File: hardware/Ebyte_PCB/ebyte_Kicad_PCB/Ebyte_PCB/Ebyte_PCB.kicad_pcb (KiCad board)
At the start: 2 copper layers, 31 parts, among them Q1 NPN, Q2 PMOS, U1 DF11, U2 LT8612IUDE, U3 E32-400M33S SX1278, U4 MIC69303RT, U5 CONMMCX001, U6 SN74LVC1G08DBVR

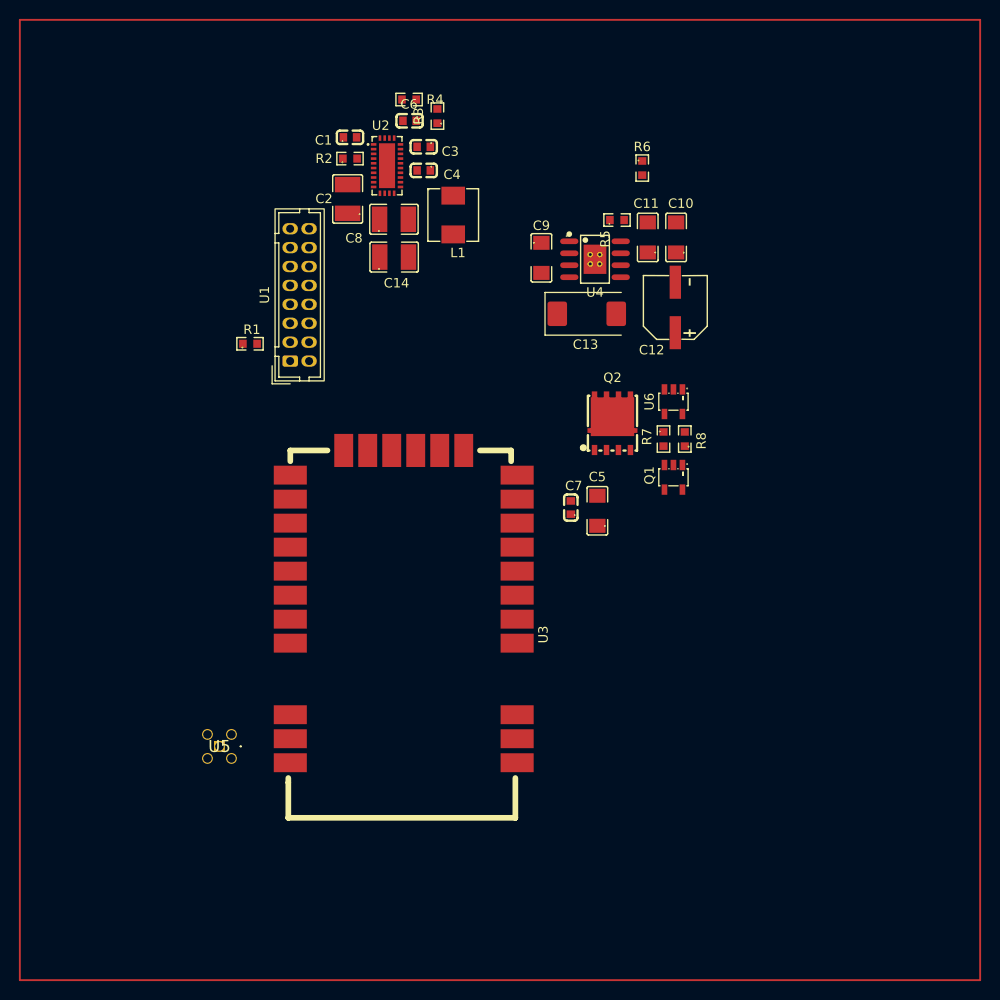
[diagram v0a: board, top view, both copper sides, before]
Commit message: Zone/Tracing v1
started zoning/tracing for buck converter
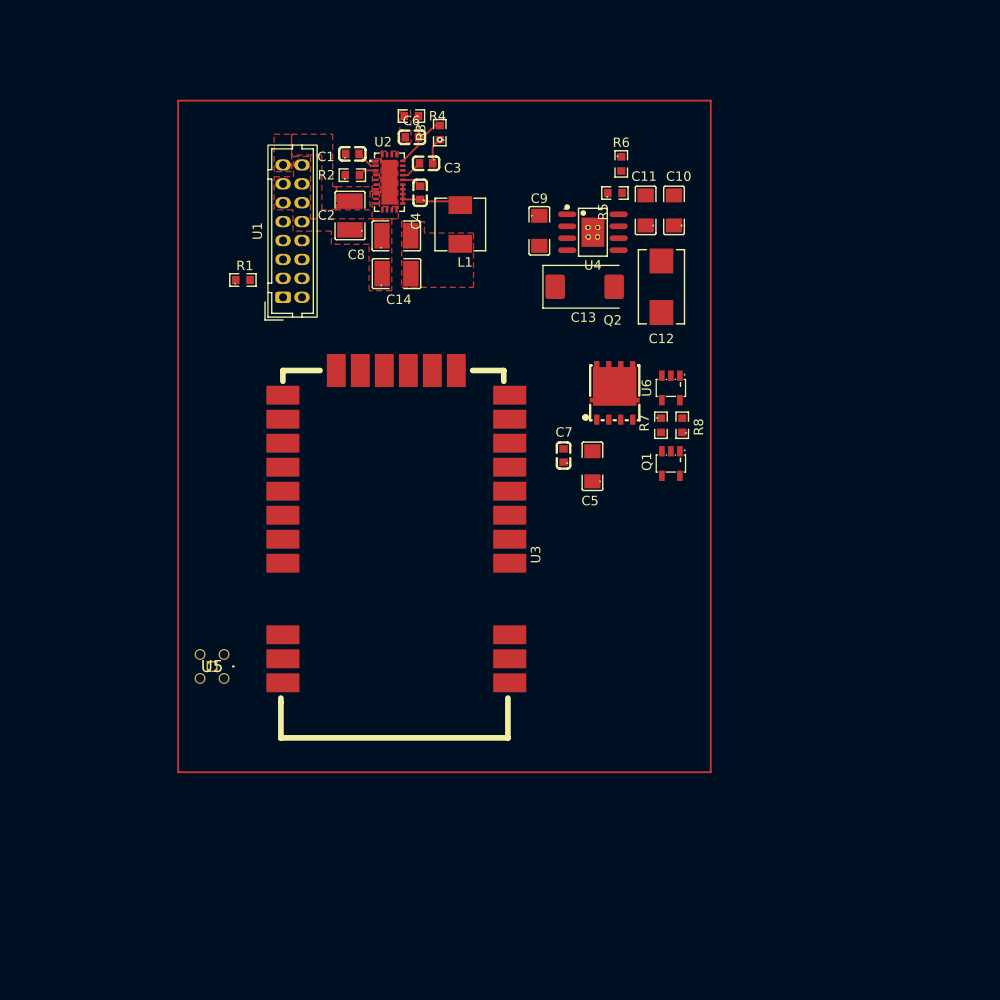
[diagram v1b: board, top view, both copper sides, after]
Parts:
- C12: footprint ebyte_footprints:CAP-SMD_BD6.3-L6.6-W6.6-FD -> ebyte_footprints:CAP_593D_D_VIS-M
- moved U5 8.49 mm to (45.7, 93.8)
- moved U3 8.49 mm to (53.5, 63.3)
- moved R1 6.79 mm to (49.0, 52.9)
- moved U1 6.79 mm to (53.2, 54.8)
- moved C7 5.56 mm to (83.2, 71.5)
- moved C5 4.74 mm to (86.0, 72.6)
- moved Q2 3.22 mm to (88.3, 64.9)
- moved C10 2.87 mm to (94.6, 45.6)
- moved C11 2.87 mm to (91.6, 45.6)
- moved C13 2.87 mm to (85.2, 53.6)
- moved C9 2.87 mm to (80.4, 47.7)
- moved R5 2.87 mm to (88.4, 43.7)
- moved U4 2.87 mm to (86.0, 47.9)
- moved C4 2.68 mm to (68.1, 43.7), turned to 90 degrees
- moved C12 2.64 mm to (93.3, 53.6)
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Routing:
- net Net-(C4-Pad1): track 0.00 -> 8.36 mm
- net Net-(U2-FB): track 0.00 -> 8.21 mm
- net GND: track 0.00 -> 2.81 mm, vias 0 -> 1
- net Net-(U2-TR/SS): track 0.00 -> 2.32 mm
- net Net-(U2-INTVCC): track 0.00 -> 2.28 mm
- net Net-(U2-BST): track 0.00 -> 2.11 mm
- net Net-(U2-RT): track 0.00 -> 1.96 mm
- added copper zone on F.Cu, net GND
- added copper zone on In1.Cu, net GND
- added copper zone on F.Cu, net Net-(U2-BIAS)
- added copper zone on F.Cu, net VIN
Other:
- copper layers 2 -> 4

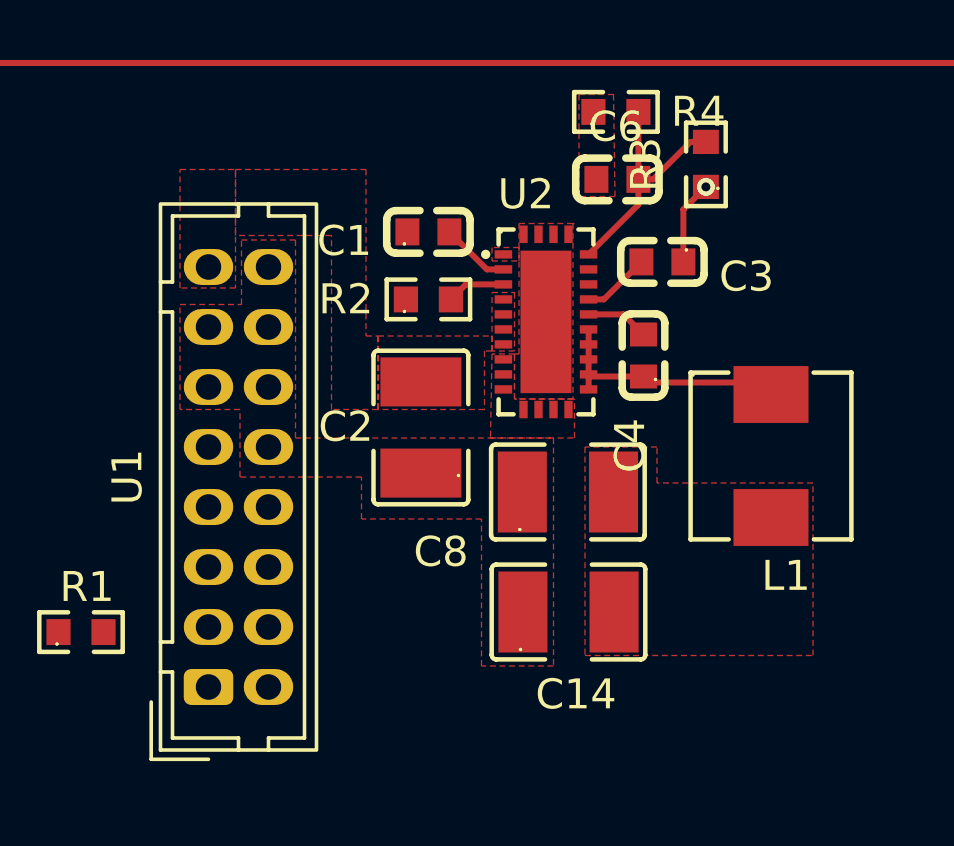
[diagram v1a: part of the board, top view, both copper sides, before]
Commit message: Review 2 update
cleaned up schematic
changed EN
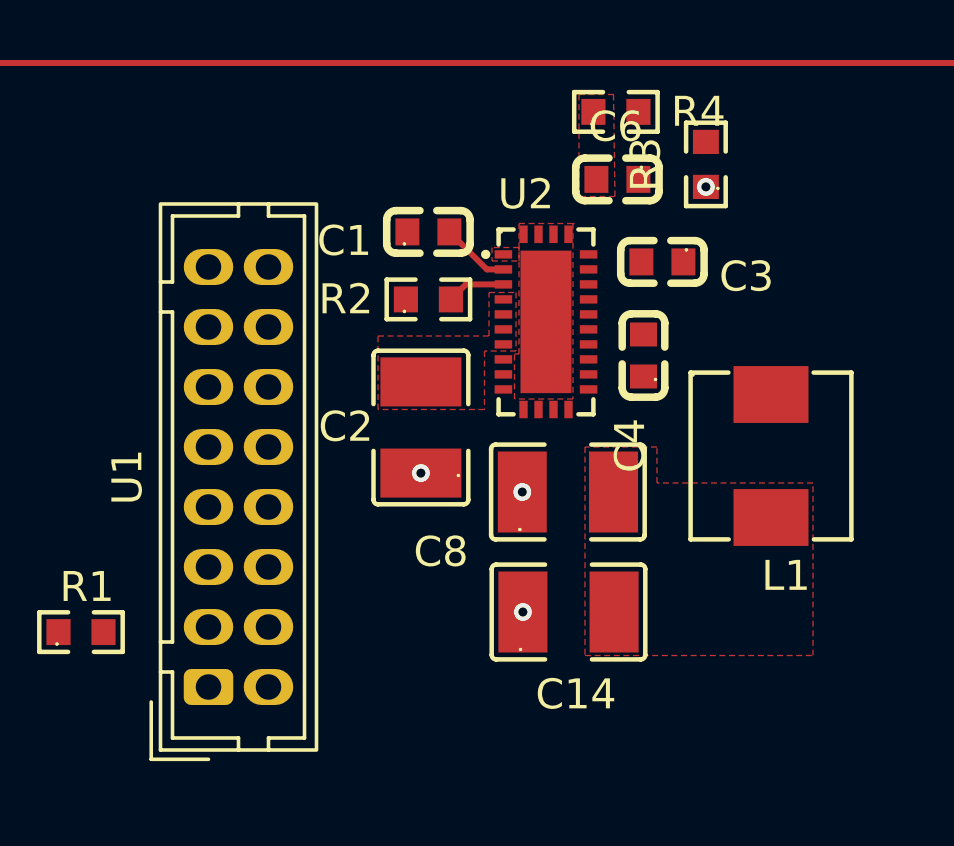
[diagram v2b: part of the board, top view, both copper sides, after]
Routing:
- net Net-(C4-Pad1): track 8.36 -> 0.00 mm
- net Net-(U2-FB): track 8.21 -> 0.00 mm
- net GND: track 2.81 -> 0.00 mm, vias 1 -> 4
- net Net-(U2-INTVCC): track 2.28 -> 0.00 mm
- net Net-(U2-BST): track 2.11 -> 0.00 mm

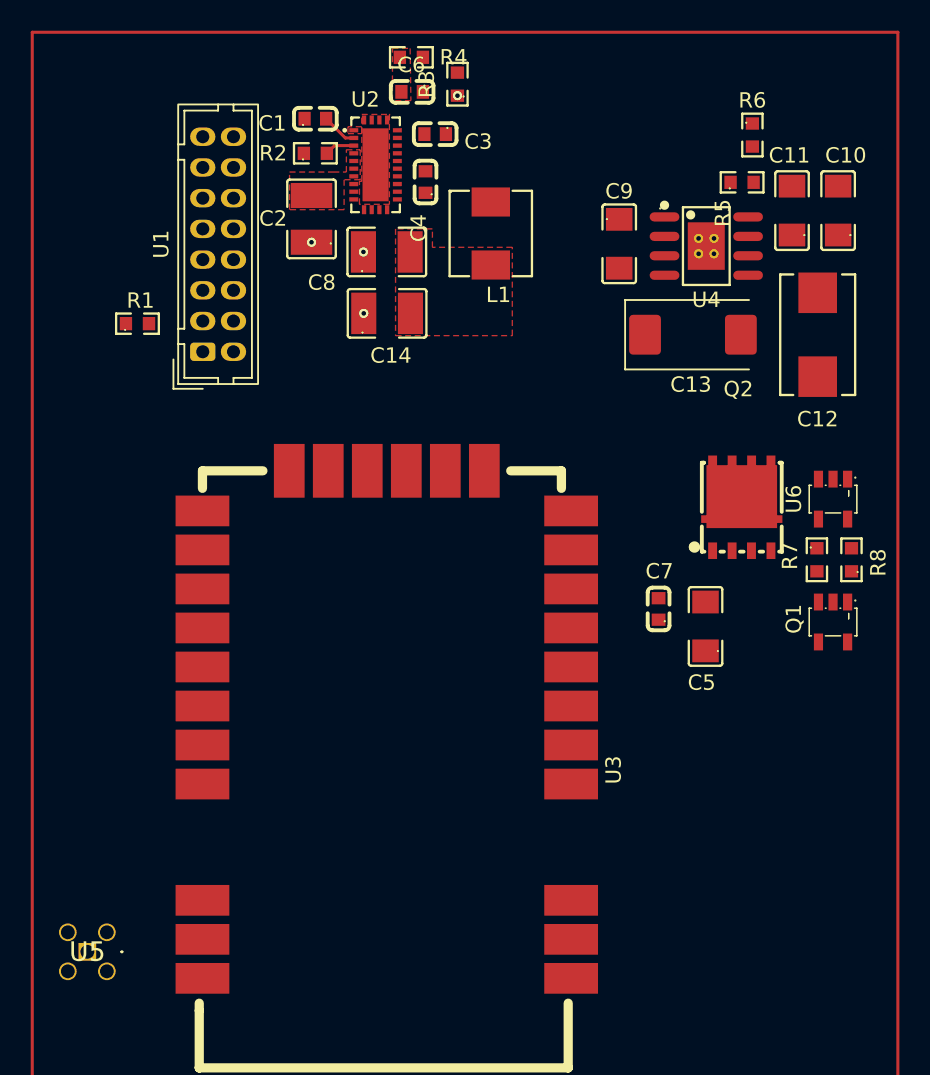
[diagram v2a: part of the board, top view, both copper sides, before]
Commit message: pcbv1
initial routing of df11, buck, ldo
have not worked on sdi
need to figure out enabling buck from cdh
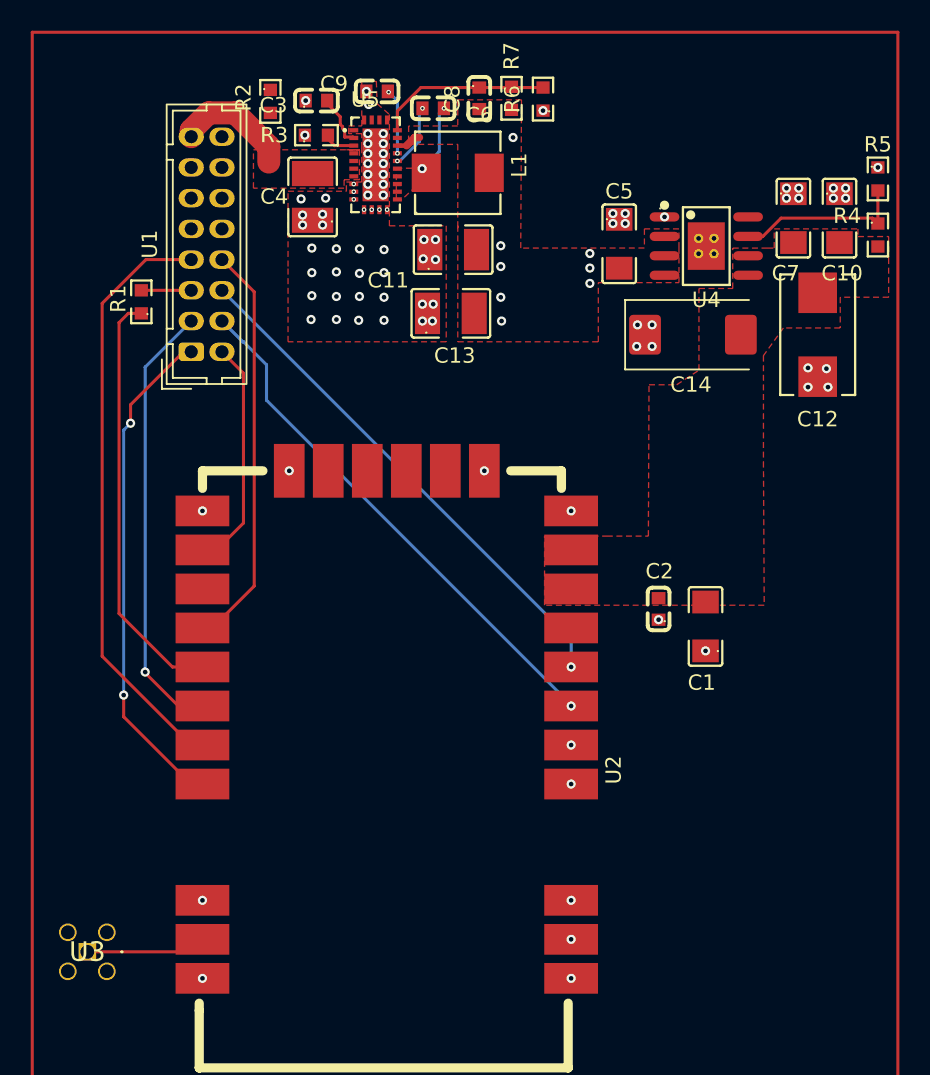
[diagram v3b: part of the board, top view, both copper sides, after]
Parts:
- removed Q1: NPN, ebyte_footprints:SOT-23-5_L3.0-W1.7-P0.95-LS2.8-BR
- removed Q2: PMOS, ebyte_footprints:DFN-8_L5.1-W5.7-P1.27-LS6.1-BL
- removed R8: 100k, ebyte_footprints:R0603
- removed U6: SN74LVC1G08DBVR, ebyte_footprints:SOT-23-5_L3.0-W1.7-P0.95-LS2.8-BR
- moved R2 46.4 mm to (57.6, 38.5)
- moved R4 9.48 mm to (97.2, 47.1), turned to -90 degrees
- moved R5 8.66 mm to (97.2, 43.5)
- moved R7 7.05 mm to (73.3, 38.2), turned to 90 degrees
- moved R6 5.65 mm to (75.4, 38.3)
- moved C6 5.11 mm to (68.2, 38.6), turned to 180 degrees
- moved L1 4.50 mm to (69.8, 43.1), turned to 0 degrees
- moved C9 4.36 mm to (64.6, 38.1), turned to 0 degrees
- moved C11 4.32 mm to (69.5, 48.1)
- moved C13 4.15 mm to (69.4, 52.2)
- moved C8 4.13 mm to (70.9, 38.2), turned to -90 degrees
- moved C10 3.13 mm to (94.7, 46.0), turned to -90 degrees
- moved C7 2.95 mm to (91.7, 46.0), turned to -90 degrees
- moved R1 1.44 mm to (49.2, 51.5), turned to 90 degrees
- moved C4 1.43 mm to (60.4, 44.7)
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- renumbered C5 to C1, C11 to C10, C8 to C11, C14 to C13, C13 to C14, C7 to C2, C1 to C3, C2 to C4, C9 to C5, C4 to C6, C10 to C7, C6 to C8, C3 to C9, R7 to R2, R2 to R3, R5 to R4, R6 to R5, R3 to R6, R4 to R7, U3 to U2, U5 to U3, U2 to U5
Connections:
- net Net-(U2-BIAS) renamed Buck_Out
- C1 pad 2: VCC -> LDO_out
- C10 pad 2: Net-(Q2-S) -> LDO_out
- C12 pad 2: Net-(Q2-S) -> LDO_out
- C14 pad 2: Net-(Q2-S) -> LDO_out
- C2 pad 2: VCC -> LDO_out
- C7 pad 2: Net-(Q2-S) -> LDO_out
- R1 pad 1: SPI1_SDO -> SPI1_SDI
- R2 pad 1: Net-(U6-Y) -> GND
- R2 pad 2: Net-(Q1-B) -> EN
- R4 pad 2: Net-(Q2-S) -> LDO_out
- U1 pad 2: GPIO1_25 -> EN
- U1 pad 3: Net-(R1-Pad2) -> SPI1_SDO
- U1 pad 5: SPI1_SDI -> Net-(R1-Pad2)
- U2 pad 10: VCC -> LDO_out
- U2 pad 19: GPIO1_25 -> EN
- U2 pad 9: VCC -> LDO_out
- U4 pad : (no net) -> GND
- U4 pad 5: Net-(Q2-S) -> LDO_out
- U4 pad 6: Net-(Q2-S) -> LDO_out
- U5 pad 4: VIN -> EN
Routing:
- net SPI1_SCK: track 0.00 -> 38.9 mm
- net RXEN: track 0.00 -> 34.5 mm, vias 0 -> 2
- net TXEN: track 0.00 -> 33.9 mm, vias 0 -> 2
- net SPI1_CS1: track 0.00 -> 32.8 mm, vias 0 -> 2
- net SPI1_SDO: track 0.00 -> 28.8 mm, vias 0 -> 2
- net SPI1_SDI: track 0.00 -> 27.5 mm
- net RST: track 0.00 -> 26.6 mm
- net EN: track 0.00 -> 15.8 mm
- net Net-(U5-FB): track 0.00 -> 11.5 mm
- net Net-(U4-ADJ): track 0.00 -> 11.2 mm
- net ANT: track 0.00 -> 7.83 mm
- net VIN: track 0.24 -> 7.86 mm
- net Net-(C6-Pad1): track 0.00 -> 6.42 mm, vias 0 -> 2
- net Net-(U5-INTVCC): track 0.00 -> 4.22 mm, vias 0 -> 2
- net Net-(U5-BST): track 0.00 -> 4.19 mm, vias 0 -> 2
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- added copper zone on In2.Cu, net Buck_Out
- added copper zone on F.Cu, net LDO_out
- added copper zone on F.Cu, net Net-(C6-Pad1)

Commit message: tracing v2
still need to do impedence matching
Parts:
- added C15: .1u, ebyte_footprints:C0603, F.Cu at (45.5, 66.8)
- added R10: 10k, ebyte_footprints:R0603, F.Cu at (57.5, 47.6)
- added R8: 10k, ebyte_footprints:R0603, F.Cu at (82.9, 75.5)
- added R9: 4.7k, ebyte_footprints:R0603, F.Cu at (83.8, 80.5)
- added U6: SN74LV1T126DBVR_buf, ebyte_footprints:SOT-23-5_L2.9-W1.6-P0.95-LS2.8-TL, F.Cu at (46.9, 70.4)
- moved R2 47.8 mm to (83.8, 78.5), turned to 180 degrees
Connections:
- R2 pad 1: GND -> PG
- R2 pad 2: EN -> Net-(U2-RXEN)
- U1 pad 10: GND -> 3v3
- U1 pad 14: GND -> VIN
- U1 pad 15: VIN -> GND
- U1 pad 16: GND -> VIN
- U1 pad 2: EN -> GPIO1_25
- U2 pad 19: EN -> GPIO1_25
- U2 pad 22: SPI1_SDI -> Net-(U2-MISO)
- U2 pad 6: RXEN -> Net-(U2-RXEN)
- U4 pad : GND -> (no net)
- U5 pad 23: unconnected-(U5-PG-Pad23) -> PG
- U5 pad 4: EN -> VIN
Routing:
- net PG: track 0.00 -> 55.2 mm, vias 0 -> 2
- net 3v3: track 0.00 -> 30.0 mm, vias 0 -> 2
- net X_PGOOD: track 0.00 -> 29.1 mm, vias 0 -> 2
- net GPIO1_25: track 0.00 -> 15.8 mm
- net EN: track 15.8 -> 0.00 mm
- net SPI1_SDI: track 27.5 -> 17.9 mm
- net Net-(U2-RXEN): track 0.00 -> 8.11 mm
- net Net-(U2-MISO): track 0.00 -> 8.09 mm
- net RXEN: track 34.5 -> 41.5 mm
- net TXEN: track 33.9 -> 40.0 mm
- net VIN: track 7.86 -> 4.60 mm
- net SPI1_SCK: track 38.9 -> 41.4 mm
- net LDO_out: vias 0 -> 14
- net GND: vias 95 -> 102
- added copper zone on In2.Cu, net GND
- added copper zone on In2.Cu, net LDO_out

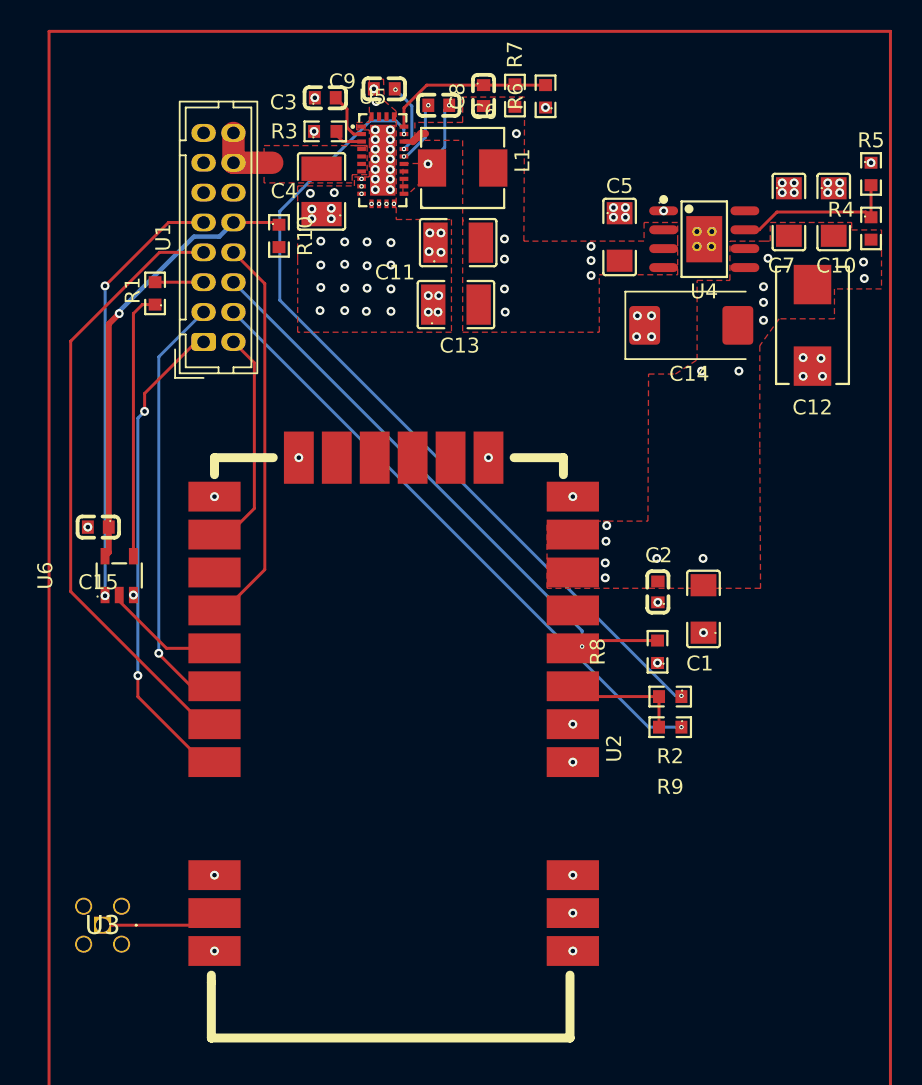
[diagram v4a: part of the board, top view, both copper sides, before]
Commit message: tracing v3
fixed vias
added impedence matching
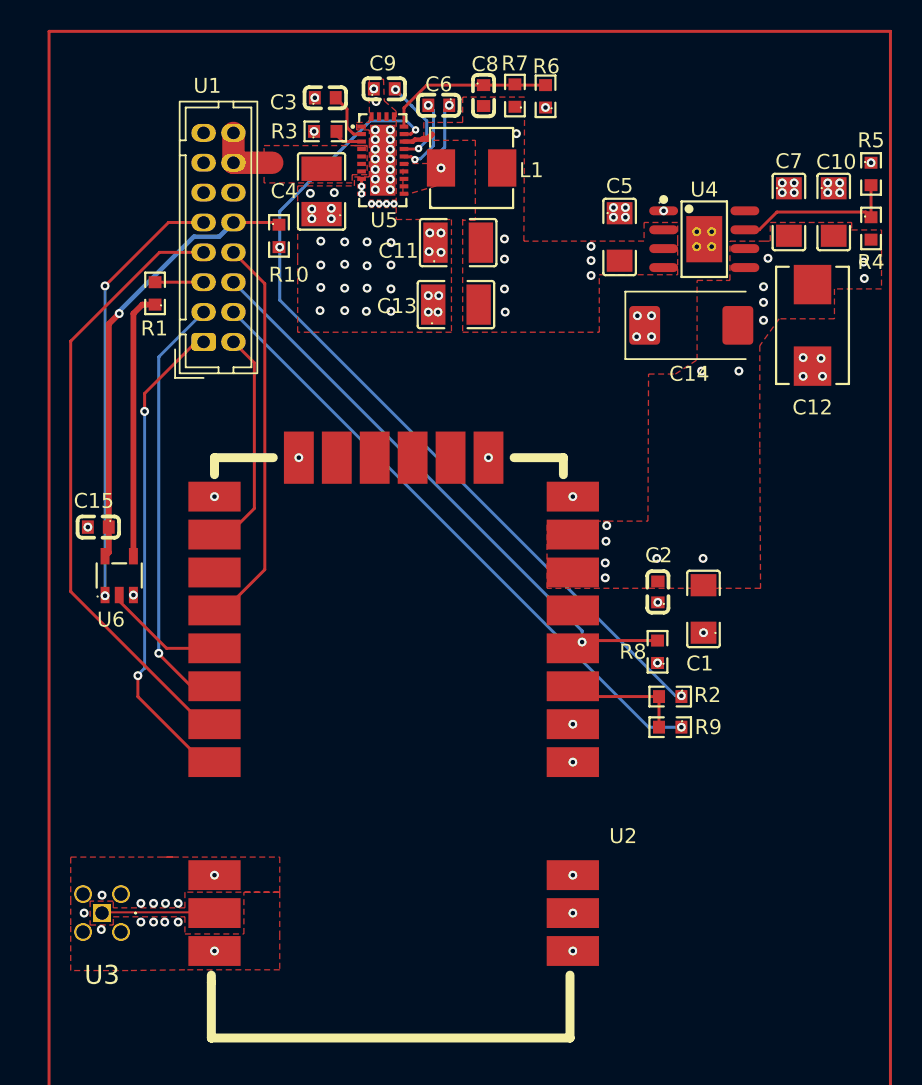
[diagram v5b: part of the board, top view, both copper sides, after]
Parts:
- moved U3 0.81 mm to (45.7, 93.0)
- moved L1 0.60 mm to (70.5, 43.1)
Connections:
- U4 pad : (no net) -> GND
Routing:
- net PG: track 55.2 -> 56.7 mm, vias 2 -> 3
- net Net-(U5-INTVCC): track 4.65 -> 6.04 mm
- net Net-(U5-BST): track 4.19 -> 5.42 mm
- net Net-(C6-Pad1): track 6.42 -> 5.28 mm
- net GND: track 0.00 -> 0.50 mm, vias 102 -> 104
- net TXEN: track 40.0 -> 39.7 mm, vias 2 -> 1
- net SPI1_SDO: vias 2 -> 1
- net RXEN: vias 2 -> 1
- net 3v3: vias 2 -> 1
